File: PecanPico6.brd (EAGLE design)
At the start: 50 x 29.8 mm, 80 parts, among them IC1 TPS79718DCKT, IC2 SI4463/4, IC3 UBLOX_MAX-6, IC4 LPC1114FHN33/333, IC5 SPV1040, IC6 AS213-92LF, IC7 BMP180, Q2 AP2301

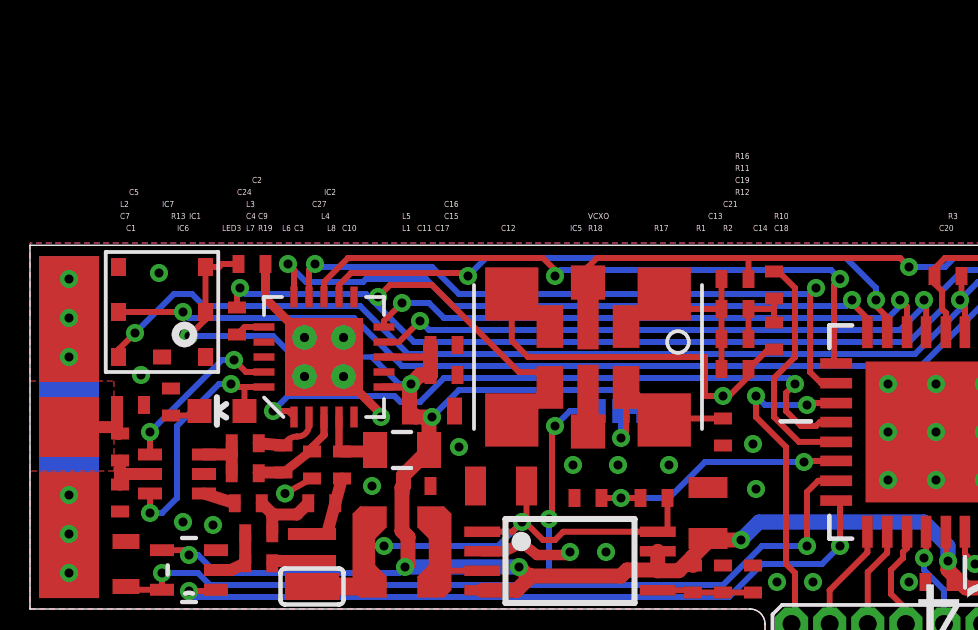
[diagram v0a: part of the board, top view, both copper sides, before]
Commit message: Changed net class restrictions, fixed DRC errors on board
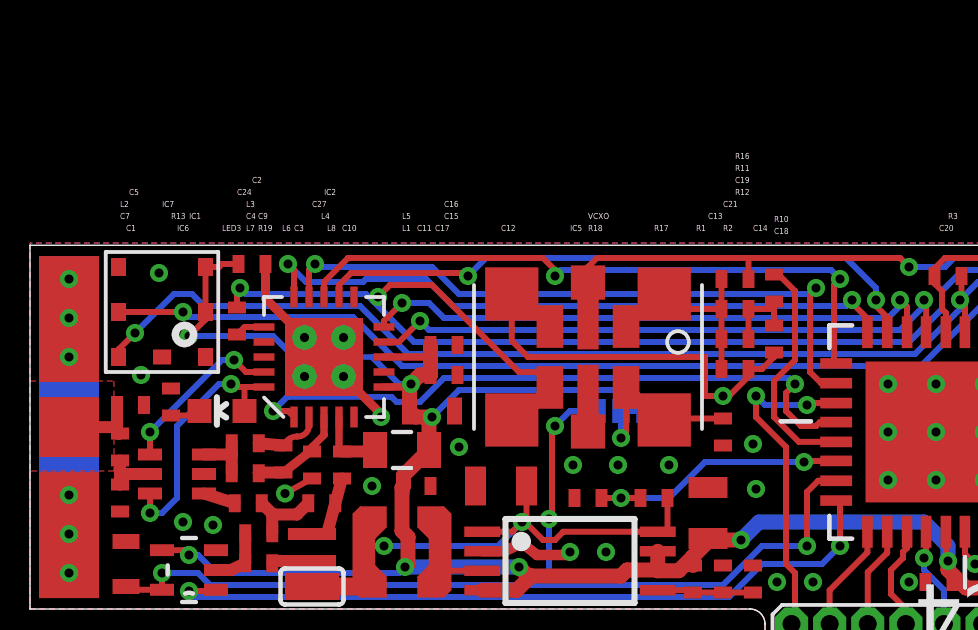
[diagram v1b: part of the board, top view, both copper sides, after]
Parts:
- moved C18 0.10 mm to (26.2, 17.7)
- moved R10 0.10 mm to (26.2, 19.4)
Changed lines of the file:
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@@
 </variantdefs>
 <classes>
-<class number="0" name="default" width="0.2032" drill="0">
-<clearance class="0" value="0.205"/>
+<class number="0" name="default" width="0.1524" drill="0.3">
+<clearance class="0" value="0.1524"/>
 </class>
-<class number="1" name="vcc" width="0.254" drill="0">
+<class number="1" name="vcc" width="0.254" drill="0.3">
+<clearance class="1" value="0.1524"/>
 </class>
 </classes>
-<designrules name="SeeedStudio_2layer_DRU_no_angle_20140221">
+<designrules name="SeeedStudio_2layer_DRU_no_angle_20140221 *">
 <description language="de">&lt;b&gt;EAGLE Design Rules&lt;/b&gt;
 &lt;p&gt;
@@
 <param name="mdSmdStop" value="0mil"/>
 <param name="msWidth" value="6mil"/>
-<param name="msDrill" value="12mil"/>
+<param name="msDrill" value="0.3mm"/>
 <param name="msMicroVia" value="12mil"/>
 <param name="msBlindViaRatio" value="0.5"/>
@@
 <attribute name="VALUE" x="9.3" y="17.6" size="0.2" layer="27" rot="R90"/>
 </element>
-<element name="C18" library="sven" package="0402" value="100nF" x="26.2" y="17.8" smashed="yes" rot="R90">
-<attribute name="NAME" x="26.2" y="21.3" size="0.2" layer="25"/>
-<attribute name="VALUE" x="27.2" y="17.1" size="0.2" layer="27" rot="R90"/>
+<element name="C18" library="sven" package="0402" value="100nF" x="26.2" y="17.7" smashed="yes" rot="R90">
+<attribute name="NAME" x="26.2" y="21.2" size="0.2" layer="25"/>
+<attribute name="VALUE" x="27.2" y="17" size="0.2" layer="27" rot="R90"/>
 </element>
 <element name="C19" library="sven" package="0402" value="56nF" x="24.9" y="17.7" smashed="yes" rot="R180">
@@
 <attribute name="VALUE" x="24.2" y="17.7" size="0.2" layer="27"/>
 </element>
-<element name="R10" library="sven" package="0402" value="300R" x="26.2" y="19.5" smashed="yes" rot="R90">
-<attribute name="NAME" x="26.2" y="21.7" size="0.2" layer="25"/>
-<attribute name="VALUE" x="27.2" y="18.8" size="0.2" layer="27" rot="R90"/>
+<element name="R10" library="sven" package="0402" value="300R" x="26.2" y="19.4" smashed="yes" rot="R90">
+<attribute name="NAME" x="26.2" y="21.6" size="0.2" layer="25"/>
+<attribute name="VALUE" x="27.2" y="18.7" size="0.2" layer="27" rot="R90"/>
 </element>
 <element name="C20" library="sven" package="0402" value="100nF" x="31.7" y="9.6" smashed="yes">
@@
 <wire x1="18.3" y1="10.5" x2="19.3" y2="10.5" width="0.35" layer="1"/>
 <wire x1="19.3" y1="10.5" x2="19.4" y2="10.6" width="0.35" layer="1"/>
-<wire x1="26.2" y1="17.35" x2="26" y2="17.35" width="0.2" layer="1"/>
-<wire x1="26" y1="17.35" x2="25.35" y2="16.7" width="0.2" layer="1"/>
 <wire x1="25.35" y1="16.7" x2="25.35" y2="16.45" width="0.2" layer="1"/>
 <wire x1="25.35" y1="16.45" x2="24.7" y2="15.8" width="0.2" layer="1"/>
@@
 <wire x1="39.1" y1="12.6" x2="37.8" y2="12.6" width="0.5" layer="16"/>
 <via x="6.5" y="11.6" extent="1-16" drill="0.3"/>
+<wire x1="25.35" y1="16.7" x2="25.8" y2="16.7" width="0.2" layer="1"/>
+<wire x1="25.8" y1="16.7" x2="26.2" y2="17.1" width="0.2" layer="1"/>
+<wire x1="26.2" y1="17.1" x2="26.2" y2="17.25" width="0.2" layer="1"/>
 </signal>
 <signal name="SCK">
@@
 <wire x1="33.3" y1="19" x2="33.5" y2="18.8" width="0.2" layer="16"/>
 <wire x1="33.5" y1="18.8" x2="36.6682" y2="18.8" width="0.2" layer="16"/>
-<wire x1="6.5" y1="18.6" x2="6.7" y2="18.4" width="0.2" layer="16"/>
-<wire x1="6.7" y1="18.4" x2="12.2" y2="18.4" width="0.2" layer="16"/>
-<wire x1="12.2" y1="18.4" x2="13.8" y2="16.8" width="0.2" layer="16"/>
+<wire x1="6.67" y1="18.43" x2="12.17" y2="18.43" width="0.2" layer="16"/>
+<wire x1="12.17" y1="18.43" x2="13.8" y2="16.8" width="0.2" layer="16"/>
+<wire x1="6.5" y1="18.6" x2="6.67" y2="18.43" width="0.2" layer="16"/>
 </signal>
 <signal name="N$21">
@@
 <wire x1="15.2" y1="16.4" x2="26.7" y2="16.4" width="0.2" layer="16"/>
 <wire x1="26.7" y1="16.4" x2="26.9" y2="16.2" width="0.2" layer="16"/>
-<wire x1="13.75" y1="15.6" x2="14.4" y2="15.6" width="0.2" layer="16"/>
+<wire x1="13.62" y1="15.6" x2="14.4" y2="15.6" width="0.2" layer="16"/>
 <wire x1="14.4" y1="15.6" x2="15.2" y2="16.4" width="0.2" layer="16"/>
 <wire x1="26.9" y1="16.2" x2="26.6" y2="15.9" width="0.2" layer="1"/>
 <wire x1="26.6" y1="15.9" x2="26.6" y2="15.3" width="0.2" layer="1"/>
 <wire x1="26.6" y1="15.3" x2="27.1" y2="14.8" width="0.2" layer="1"/>
-<wire x1="13.75" y1="15.6" x2="13.55" y2="15.8" width="0.2" layer="16"/>
-<wire x1="10" y1="15.8" x2="9.5" y2="15.3" width="0.2" layer="16"/>
 <wire x1="27.1" y1="14.8" x2="27.6" y2="14.8" width="0.2" layer="1"/>
 <wire x1="27.6" y1="14.8" x2="27.7302" y2="14.9302" width="0.2" layer="1"/>
 <wire x1="27.7302" y1="14.9302" x2="28.2726" y2="14.9302" width="0.2" layer="1"/>
-<wire x1="10" y1="15.8" x2="13.55" y2="15.8" width="0.2" layer="16"/>
+<wire x1="9.97" y1="15.77" x2="13.45" y2="15.77" width="0.2" layer="16"/>
+<wire x1="13.45" y1="15.77" x2="13.62" y2="15.6" width="0.2" layer="16"/>
+<wire x1="9.5" y1="15.3" x2="9.97" y2="15.77" width="0.2" layer="16"/>
 </signal>
 <signal name="N$13">
@@
 <contactref element="R11" pad="P$2"/>
 <contactref element="R10" pad="P$1"/>
-<wire x1="26.2" y1="18.7" x2="26.2" y2="18.25" width="0.2" layer="1"/>
+<wire x1="26.2" y1="18.7" x2="26.2" y2="18.15" width="0.2" layer="1"/>
 <wire x1="25.35" y1="17.7" x2="25.35" y2="18.7" width="0.2" layer="1"/>
 <wire x1="25.35" y1="18.7" x2="26.2" y2="18.7" width="0.2" layer="1"/>
-<wire x1="26.2" y1="18.7" x2="26.2" y2="19.05" width="0.2" layer="1"/>
+<wire x1="26.2" y1="18.7" x2="26.2" y2="18.95" width="0.2" layer="1"/>
 </signal>
 <signal name="TX_EN">
@@
 <wire x1="27.0302" y1="14.2698" x2="28.2726" y2="14.2698" width="0.2" layer="1"/>
 <wire x1="26.2" y1="15.1" x2="27.0302" y2="14.2698" width="0.2" layer="1"/>
-<wire x1="26.2" y1="19.95" x2="26.35" y2="19.95" width="0.2" layer="1"/>
-<wire x1="26.35" y1="19.95" x2="26.9" y2="19.4" width="0.2" layer="1"/>
-<wire x1="26.9" y1="19.4" x2="26.9" y2="17.1" width="0.2" layer="1"/>
-<wire x1="26.2" y1="16.4" x2="26.2" y2="15.1" width="0.2" layer="1"/>
-<wire x1="26.9" y1="17.1" x2="26.2" y2="16.4" width="0.2" layer="1"/>
+<wire x1="26.2" y1="19.85" x2="26.35" y2="19.85" width="0.2" layer="1"/>
+<wire x1="26.35" y1="19.85" x2="26.9" y2="19.3" width="0.2" layer="1"/>
+<wire x1="26.9" y1="19.3" x2="26.9" y2="17" width="0.2" layer="1"/>
+<wire x1="26.2" y1="16.3" x2="26.2" y2="15.1" width="0.2" layer="1"/>
+<wire x1="26.9" y1="17" x2="26.2" y2="16.3" width="0.2" layer="1"/>
 </signal>
 <signal name="N$5">

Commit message: Corrected 'UART TXD,RXD switched' error
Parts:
- moved SJ1 1.30 mm to (42.1, 10.7)
- moved SJ2 1.30 mm to (42.1, 9.50)
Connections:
- net RXD: now also SJ2.2; no longer SJ1.2
- net TXD: now also SJ1.2; no longer SJ2.2
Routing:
- net N$20: track 2.65 -> 6.21 mm
- net N$5: track 18.1 -> 16.9 mm
- net N$15: track 3.66 -> 2.82 mm
- net N$8: track 10.8 -> 11.4 mm
- net TXD: track 11.4 -> 10.9 mm
- net RXD: track 14.5 -> 14.0 mm
- net GND: vias 55 -> 54
